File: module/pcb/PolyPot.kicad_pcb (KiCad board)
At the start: 2 copper layers, 50 x 50 mm, 42 parts, among them J1 V_BAT_1S, J2 PROG/DEBUG, J3 HUMIDITY_CONN, J4 TOF_DIST_SENS, J5 M3, J6 M3, J7 M3, J8 M3, J9 LUMINOSITY_CONN, M1 DC_WATER_PUMP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

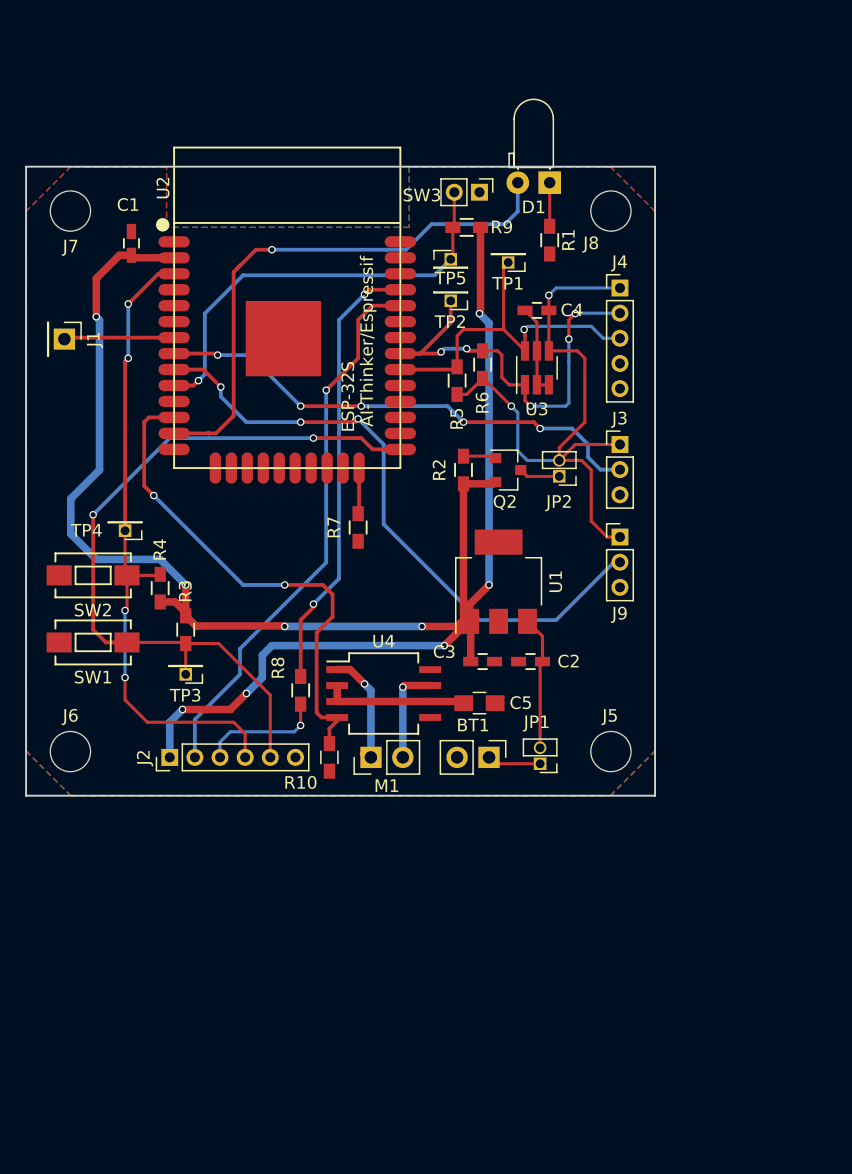
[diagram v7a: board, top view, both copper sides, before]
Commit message: PCB: Update footprints, schematic fixes, nicer edge cut, no GND next to antenna
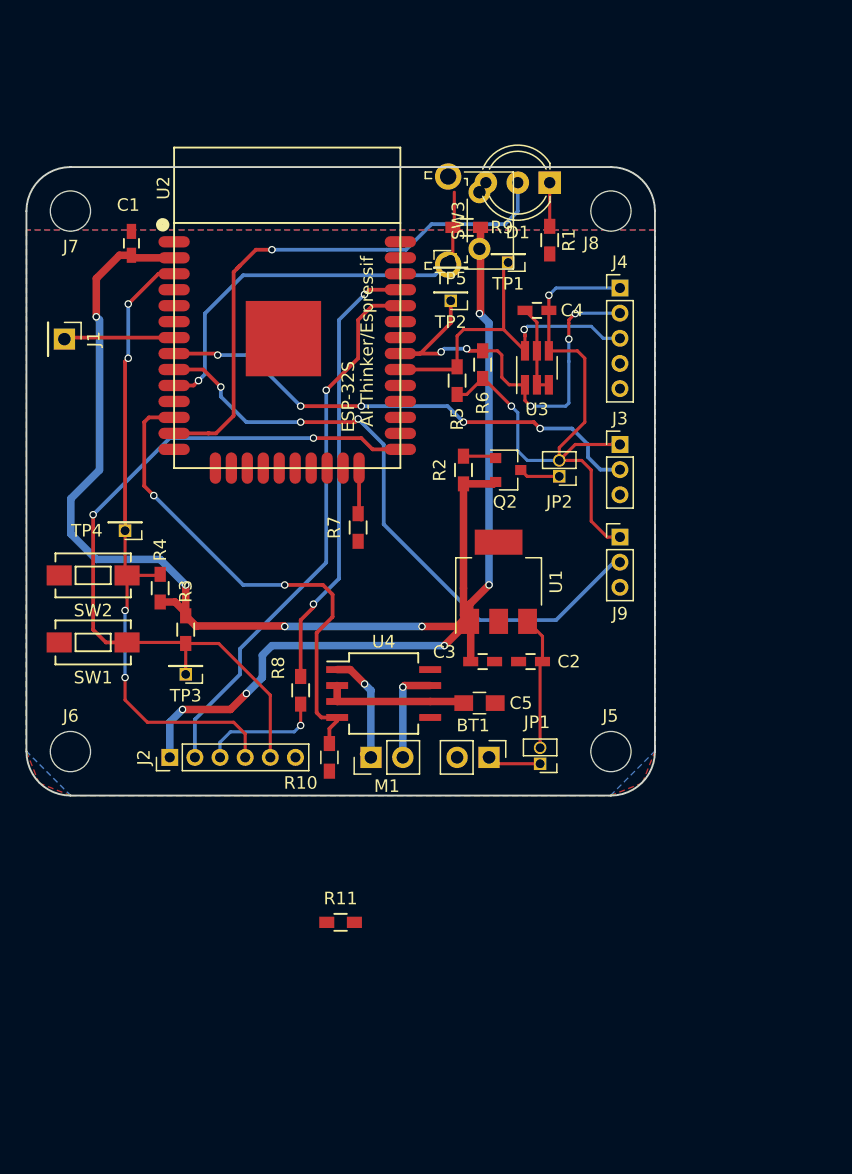
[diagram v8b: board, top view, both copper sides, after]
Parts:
- added R11: 470, Resistors_SMD:R_0603_HandSoldering, F.Cu at (55.0, 90.1)
- D1: value LED -> LED_Dual_ACA; footprint LEDs:LED_D3.0mm_Horizontal_O1.27mm_Z2.0mm -> LEDs:LED_D5.0mm-3
- R1: value 1k -> 470
- SW3: footprint Socket_Strips:Socket_Strip_Straight_1x02_Pitch2.00mm -> Buttons_Switches_THT:SW_Tactile_SPST_Angled_PTS645Vx83-2LFS
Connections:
- BT1 pad 1: Net-(BT1-Pad1) -> +BATT
- C5 pad 1: /+BATT -> +BATT
- D1 pad 2: /LED_STATUS -> GND
- J4 pad 4: /TOF_GPIO0 -> (no net)
- J5 pad 1: Net-(J5-Pad1) -> (no net)
- J6 pad 1: Net-(J6-Pad1) -> (no net)
- J7 pad 1: Net-(J7-Pad1) -> (no net)
- J8 pad 1: Net-(J8-Pad1) -> (no net)
- JP1 pad 1: Net-(BT1-Pad1) -> +BATT
- R1 pad 2: GND -> /LED_RED
- U2 pad 11: Net-(U2-Pad11) -> (no net)
- U2 pad 13: /LED_STATUS -> (no net)
- U2 pad 14: /SENSOR_ENn -> (no net)
- U2 pad 16: Net-(U2-Pad16) -> (no net)
- U2 pad 17: Net-(U2-Pad17) -> (no net)
- U2 pad 18: Net-(U2-Pad18) -> (no net)
- U2 pad 19: Net-(U2-Pad19) -> (no net)
- U2 pad 20: Net-(U2-Pad20) -> (no net)
- U2 pad 21: Net-(U2-Pad21) -> (no net)
- U2 pad 22: Net-(U2-Pad22) -> (no net)
- U2 pad 23: Net-(U2-Pad23) -> (no net)
- U2 pad 26: Net-(U2-Pad26) -> (no net)
- U2 pad 27: Net-(U2-Pad27) -> (no net)
- U2 pad 28: Net-(U2-Pad28) -> (no net)
- U2 pad 29: Net-(U2-Pad29) -> (no net)
- U2 pad 32: Net-(U2-Pad32) -> (no net)
- U2 pad 33: Net-(U2-Pad33) -> (no net)
- U2 pad 36: Net-(U2-Pad36) -> /LED_GREEN
- U2 pad 37: Net-(U2-Pad37) -> /LED_RED
- U2 pad 4: Net-(U2-Pad4) -> (no net)
- U2 pad 5: Net-(U2-Pad5) -> (no net)
- U2 pad 6: Net-(U2-Pad6) -> (no net)
- U4 pad 2: /+BATT -> +BATT
- U4 pad 3: /+BATT -> +BATT
- U4 pad 6: /+BATT -> +BATT
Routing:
- net GND: track 7.48 -> 51.6 mm, vias 0 -> 1
- net /LED_STATUS: track 44.1 -> 0.00 mm, vias 1 -> 0
- net +BATT: track 0.00 -> 15.7 mm
- net /+BATT: track 11.4 -> 0.00 mm
- net Net-(BT1-Pad1): track 4.27 -> 0.00 mm
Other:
- outline, holes or cut-outs redrawn
